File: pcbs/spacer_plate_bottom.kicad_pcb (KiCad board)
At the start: 2 copper layers, 73 x 111 mm, 0 parts

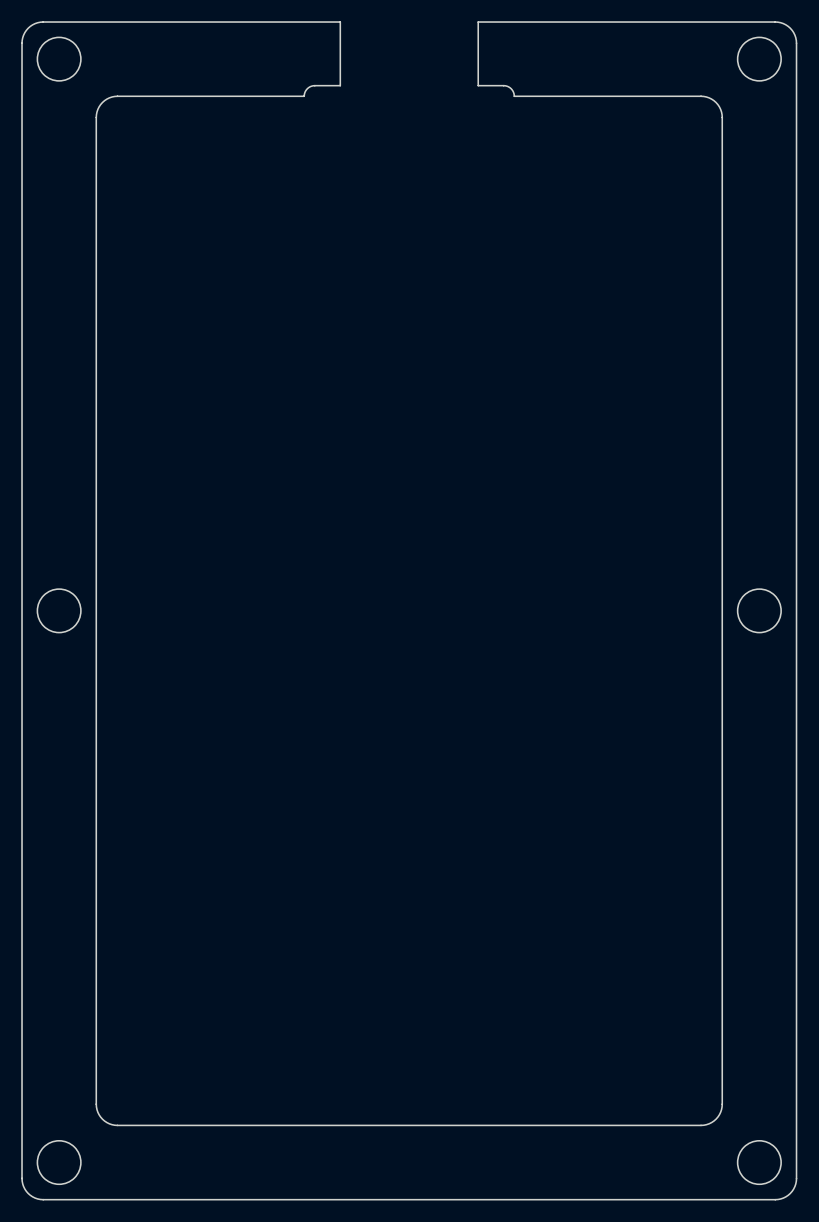
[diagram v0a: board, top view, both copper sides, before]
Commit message: Update MX switch footprint
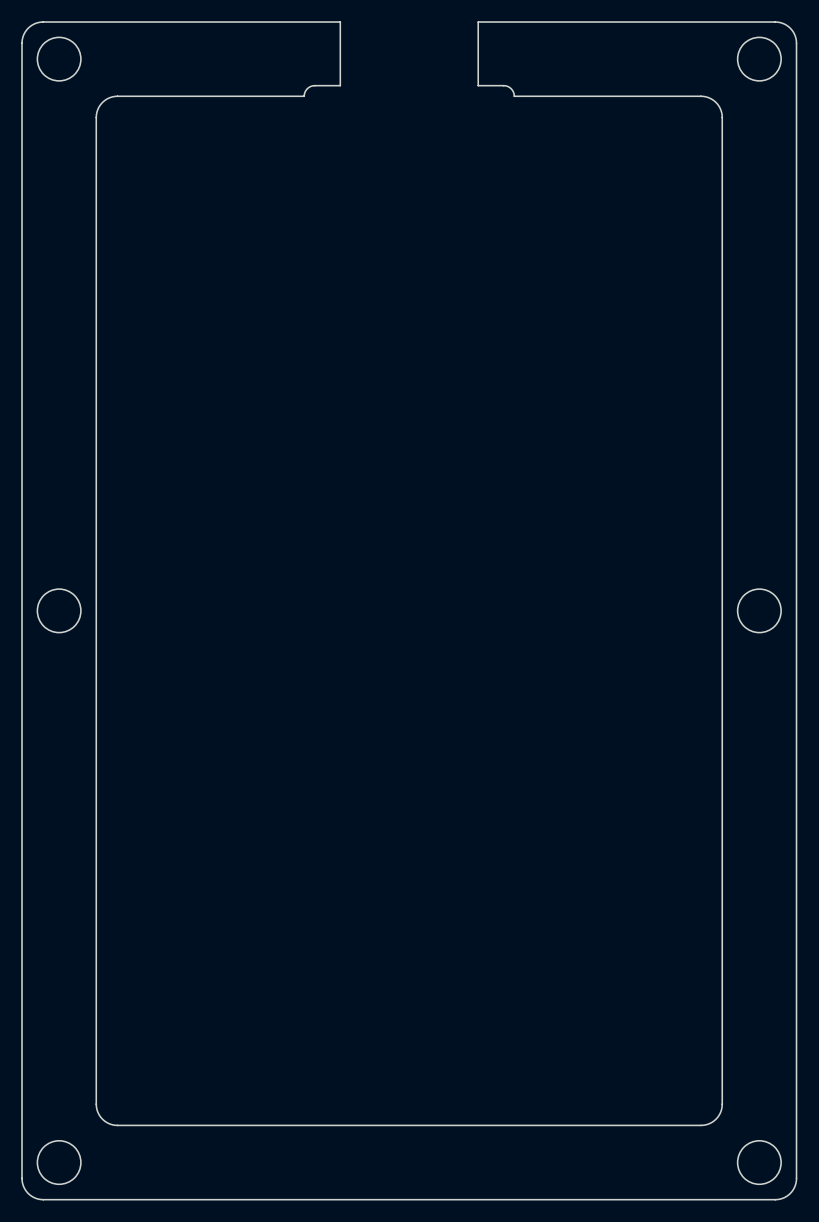
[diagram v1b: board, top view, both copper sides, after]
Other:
- net class Default removed
